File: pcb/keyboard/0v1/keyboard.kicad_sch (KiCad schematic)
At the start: 14 parts, among them U2 MDBT50Q-P1MV2, Y1 32.768

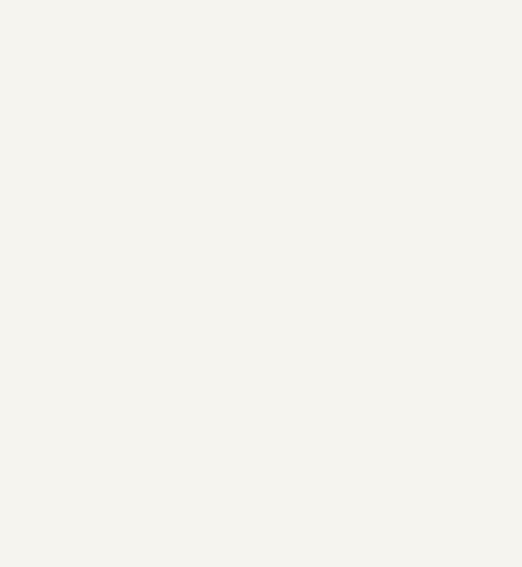
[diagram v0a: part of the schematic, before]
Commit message: Found part numbers for button and diode in the keyboard matrix
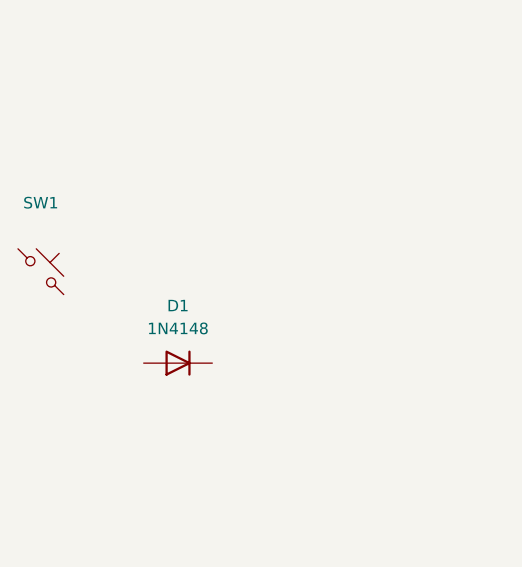
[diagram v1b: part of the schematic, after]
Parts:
- added D1: 1N4148, Diode_SMD:D_SOD-523, symbol Device:D
- added SW1: C&K PTS647SM50SMTR2LFS, symbol Switch:SW_Push_45deg
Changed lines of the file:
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@@
+	)
+	(symbol
+		(lib_id "Device:D")
+		(at 152.4 125.73 180)
+		(unit 1)
+		(exclude_from_sim no)
+		(in_bom yes)
+		(on_board yes)
+		(dnp no)
+		(fields_autoplaced yes)
+		(property "Reference" "D1"
+			(at 152.4 119.38 0)
+			(effects
+				(font
+					(size 1.27 1.27)
+				)
+			)
+		)
+		(property "Value" "1N4148"
+			(at 152.4 121.92 0)
+			(effects
+				(font
+					(size 1.27 1.27)
+				)
+			)
+		)
+		(property "Footprint" "Diode_SMD:D_SOD-523"
+			(at 152.4 125.73 0)
+			(effects
+				(font
+					(size 1.27 1.27)
+				)
+				(hide yes)
+			)
+		)
+		(property "Datasheet" "https://www.lcsc.com/datasheet/C30584800.pdf"
+			(at 152.4 125.73 0)
+			(effects
+				(font
+					(size 1.27 1.27)
+				)
+				(hide yes)
+			)
+		)
+		(property "Description" "Diode Independent 75V 150mA Surface Mount 0603"
+			(at 152.4 125.73 0)
+			(effects
+				(font
+					(size 1.27 1.27)
+				)
+				(hide yes)
+			)
+		)
+		(property "Sim.Device" "D"
+			(at 152.4 125.73 0)
+			(effects
+				(font
+					(size 1.27 1.27)
+				)
+				(hide yes)
+			)
+		)
+		(property "Sim.Pins" "1=K 2=A"
+			(at 152.4 125.73 0)
+			(effects
+				(font
+					(size 1.27 1.27)
+				)
+				(hide yes)
+			)
+		)
+		(property "Manufacturer" "YONGYUTAI"
+			(at 152.4 125.73 0)
+			(effects
+				(font
+					(size 1.27 1.27)
+				)
+				(hide yes)
+			)
+		)
+		(property "Mfr. Part no." "CD4148WTP"
+			(at 152.4 125.73 0)
+			(effects
+				(font
+					(size 1.27 1.27)
+				)
+				(hide yes)
+			)
+		)
+		(property "LCSC Part no." "C30584800"
+			(at 152.4 125.73 0)
+			(effects
+				(font
+					(size 1.27 1.27)
+				)
+				(hide yes)
+			)
+		)
+		(property "Distributor Link" "https://www.lcsc.com/product-detail/C30584800.html"
+			(at 152.4 125.73 0)
+			(effects
+				(font
+					(size 1.27 1.27)
+				)
+				(hide yes)
+			)
+		)
+		(pin "1"
+		)
+		(pin "2"
+		)
+		(instances
+			(project ""
+				(path "/c19feaf6-aecc-4469-9f12-5cd065a0782d"
+					(reference "D1")
+					(unit 1)
+				)
+			)
+		)
 	)
 	(symbol
@@
 					(unit 1)
 				)
+			)
+		)
+	)
+	(symbol
+		(lib_id "Switch:SW_Push_45deg")
+		(at 137.16 115.57 0)
+		(unit 1)
+		(exclude_from_sim no)
+		(in_bom yes)
+		(on_board yes)
+		(dnp no)
+		(fields_autoplaced yes)
+		(property "Reference" "SW1"
+			(at 137.16 107.95 0)
+			(effects
+				(font
+					(size 1.27 1.27)
+				)
+			)
+		)
+		(property "Value" "C&K PTS647SM50SMTR2LFS"
+			(at 137.16 110.49 0)
+			(effects
+				(font
+					(size 1.27 1.27)
+				)
+				(hide yes)
+			)
+		)
+		(property "Footprint" ""
+			(at 137.16 115.57 0)
+			(effects
+				(font
+					(size 1.27 1.27)
+				)
+				(hide yes)
+			)
+		)
+		(property "Datasheet" "https://www.lcsc.com/datasheet/C2689518.pdf"
+			(at 137.16 115.57 0)
+			(effects
+				(font
+					(size 1.27 1.27)
+				)
+				(hide yes)
+			)
+		)
+		(property "Description" "Tactile Switch SPST-NO 180gf Gull Wing Surface Mount"
+			(at 137.16 115.57 0)
+			(effects
+				(font
+					(size 1.27 1.27)
+				)
+				(hide yes)
+			)
+		)
+		(property "Manufacturer" "C&K"
+			(at 137.16 115.57 0)
+			(effects
+				(font
+					(size 1.27 1.27)
+				)
+				(hide yes)
+			)
+		)
+		(property "Mfr. Part no." "PTS647SM50SMTR2LFS"
+			(at 137.16 115.57 0)
+			(effects
+				(font
+					(size 1.27 1.27)
+				)
+				(hide yes)
+			)
+		)
+		(property "LCSC Part no." "C2689518"
+			(at 137.16 115.57 0)
+			(effects
+				(font
+					(size 1.27 1.27)
+				)
+				(hide yes)
+			)
+		)
+		(property "Distributor Link" "https://www.lcsc.com/product-detail/C2689518.html?s_z=n_4.5mm%20push%20button%20SMT"
+			(at 137.16 115.57 0)
+			(effects
+				(font
+					(size 1.27 1.27)
+				)
+				(hide yes)
+			)
+		)
+		(pin "1"
+		)
+		(pin "2"
+		)
+		(instances
+			(project ""
+				(path "/c19feaf6-aecc-4469-9f12-5cd065a0782d"
+					(reference "SW1")
+					(unit 1)
+				)
